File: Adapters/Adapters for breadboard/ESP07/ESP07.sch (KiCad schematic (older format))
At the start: 2 parts, among them J1 Conn_02x08_Counter_Clockwise

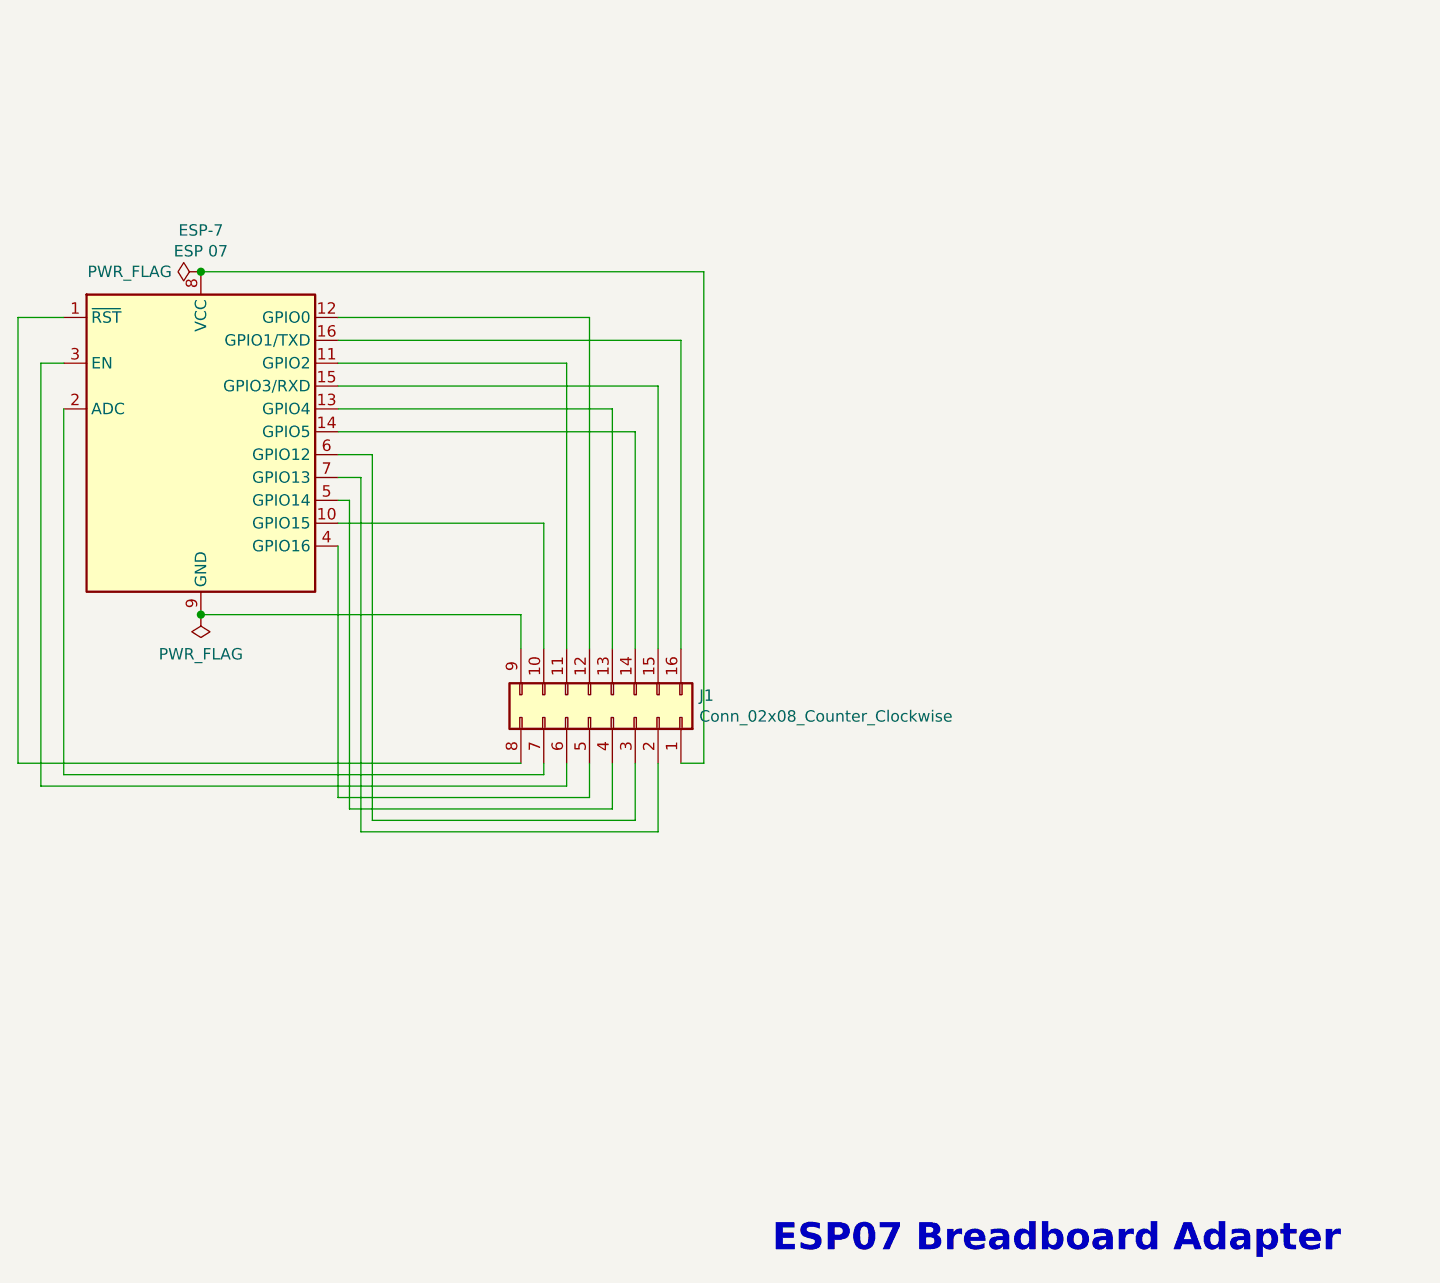
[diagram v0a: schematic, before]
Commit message: Fixed error in ESP breadboard adapter footprint, updated the schema to wire the for the new layout. Updated the ESP flashing adapter.
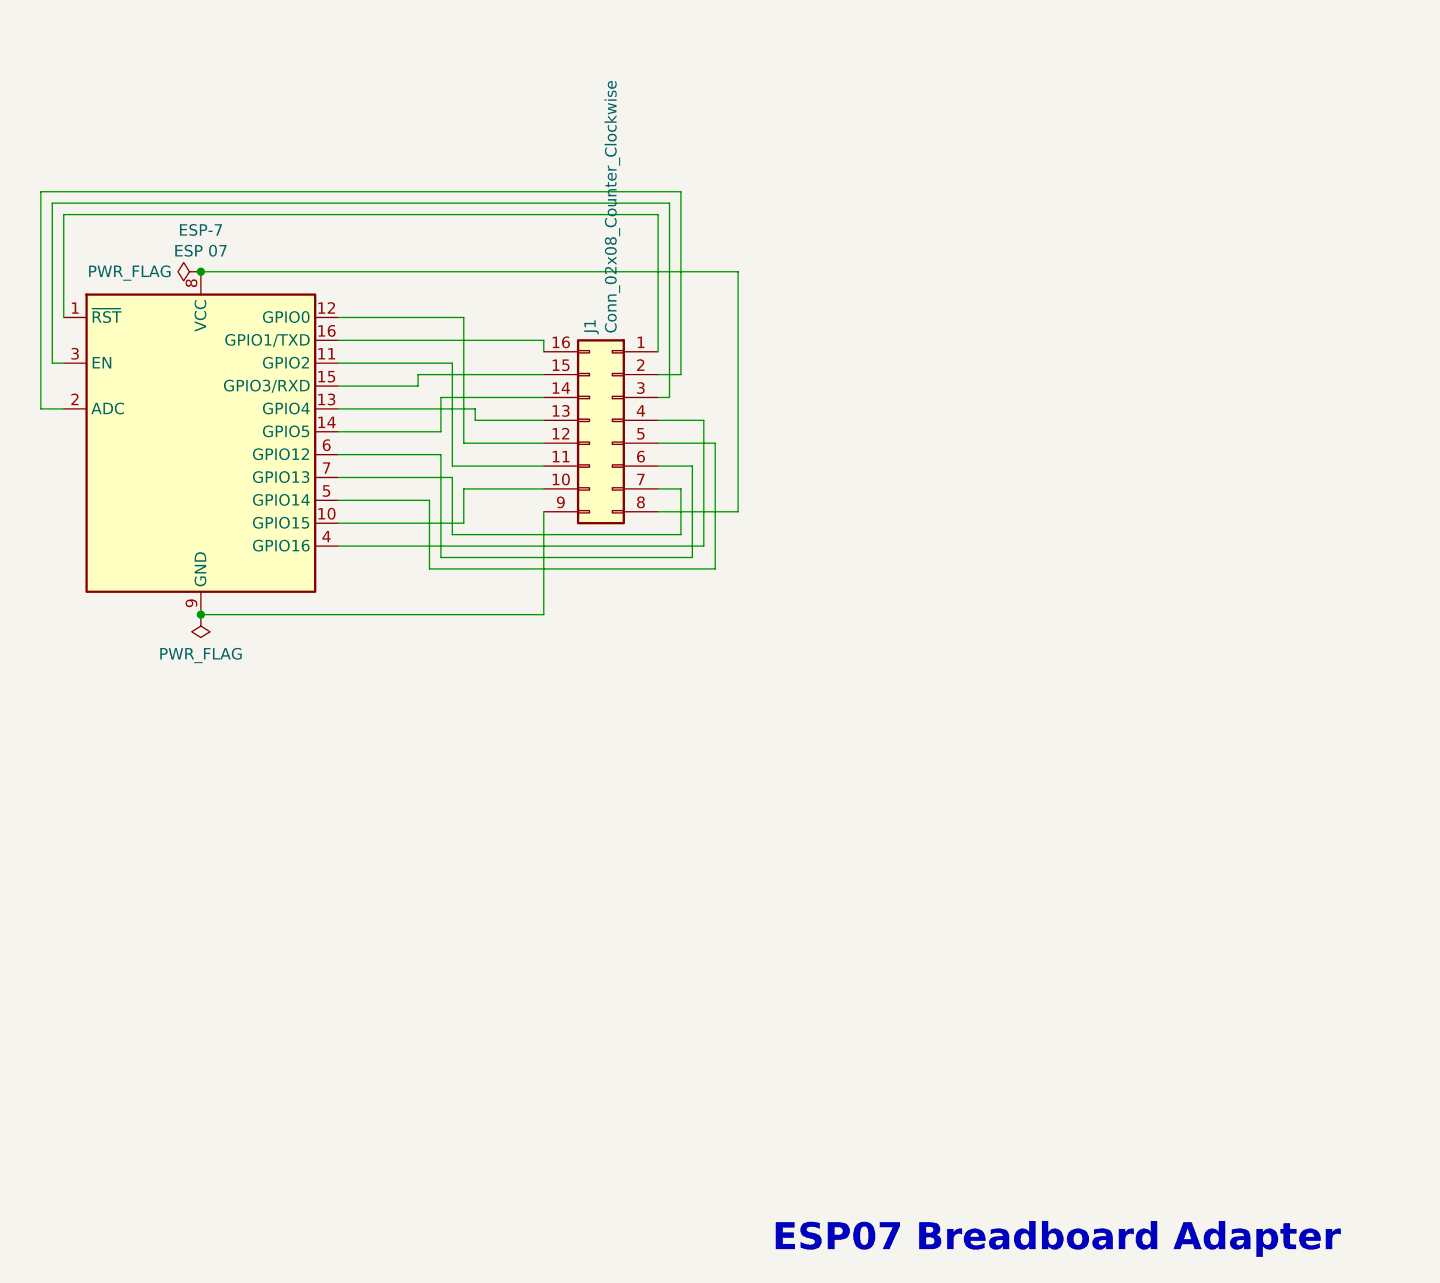
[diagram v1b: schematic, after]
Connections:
- net at ESP-7.1 (~RST): now also J1.1 (Pin_1); no longer J1.8 (Pin_8)
- net at ESP-7.2 (ADC): now also J1.2 (Pin_2); no longer J1.7 (Pin_7)
- net at ESP-7.3 (EN): now also J1.3 (Pin_3); no longer J1.6 (Pin_6)
- net at ESP-7.4 (GPIO16): now also J1.4 (Pin_4); no longer J1.5 (Pin_5)
- net at ESP-7.5 (GPIO14): now also J1.5 (Pin_5); no longer J1.4 (Pin_4)
- net at ESP-7.6 (GPIO12): now also J1.6 (Pin_6); no longer J1.3 (Pin_3)
- net at ESP-7.7 (GPIO13): now also J1.7 (Pin_7); no longer J1.2 (Pin_2)
- net at ESP-7.8 (VCC): now also J1.8 (Pin_8); no longer J1.1 (Pin_1)
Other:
- moved on the sheet: J1
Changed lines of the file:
@@
 L Connector_Generic:Conn_02x08_Counter_Clockwise J1
 U 1 1 5E50BF8B
-P 6300 4500
-F 0 "J1" V 6396 4880 50  0000 L CNN
-F 1 "Conn_02x08_Counter_Clockwise" V 6305 4880 50  0000 L CNN
-F 2 "ArduinoUnoMultiProgrammerAdapters:ESP07BreaboardSocket" H 6300 4500 50  0001 C CNN
-F 3 "~" H 6300 4500 50  0001 C CNN
-	1    6300 4500
-	0    1    -1   0
+P 6300 3200
+F 0 "J1" V 6396 3580 50  0000 L CNN
+F 1 "Conn_02x08_Counter_Clockwise" V 6305 3580 50  0000 L CNN
+F 2 "ArduinoUnoMultiProgrammerAdapters:ESP07BreaboardSocket" H 6300 3200 50  0001 C CNN
+F 3 "~" H 6300 3200 50  0001 C CNN
+	1    6300 3200
+	-1   0    0    -1
 $EndComp
 Wire Wire Line
-	4500 4050 5900 4050
+	3900 2750 3900 2300
 Wire Wire Line
-	5900 4050 5900 4200
+	3900 2300 6500 2300
+Wire Wire Line
+	6500 2300 6500 2900
+Wire Wire Line
+	3900 2950 3850 2950
+Wire Wire Line
+	3850 2950 3850 2250
+Wire Wire Line
+	3850 2250 6550 2250
+Wire Wire Line
+	6550 2250 6550 3100
+Wire Wire Line
+	6550 3100 6500 3100
+Wire Wire Line
+	3900 3150 3800 3150
+Wire Wire Line
+	3800 3150 3800 2200
+Wire Wire Line
+	3800 2200 6600 2200
+Wire Wire Line
+	6600 2200 6600 3000
+Wire Wire Line
+	6600 3000 6500 3000
+Wire Wire Line
+	5100 3750 6700 3750
+Wire Wire Line
+	6700 3750 6700 3200
+Wire Wire Line
+	6700 3200 6500 3200
+Wire Wire Line
+	5100 3550 5500 3550
+Wire Wire Line
+	5500 3550 5500 3850
+Wire Wire Line
+	5500 3850 6750 3850
+Wire Wire Line
+	6750 3850 6750 3300
+Wire Wire Line
+	6750 3300 6500 3300
+Wire Wire Line
+	5100 3350 5550 3350
+Wire Wire Line
+	5550 3350 5550 3800
+Wire Wire Line
+	5550 3800 6650 3800
+Wire Wire Line
+	6650 3800 6650 3400
+Wire Wire Line
+	6650 3400 6500 3400
+Wire Wire Line
+	5100 3450 5600 3450
+Wire Wire Line
+	5600 3450 5600 3700
+Wire Wire Line
+	5600 3700 6600 3700
+Wire Wire Line
+	6600 3700 6600 3500
+Wire Wire Line
+	6600 3500 6500 3500
+Wire Wire Line
+	4500 2550 6850 2550
+Wire Wire Line
+	6850 2550 6850 3600
+Wire Wire Line
+	6850 3600 6500 3600
+Connection ~ 4500 2550
+Wire Wire Line
+	5100 3650 5650 3650
+Wire Wire Line
+	5650 3650 5650 3500
+Wire Wire Line
+	5650 3500 6000 3500
+Wire Wire Line
+	4500 4050 6000 4050
+Wire Wire Line
+	6000 4050 6000 3600
 Connection ~ 4500 4050
 Wire Wire Line
-	5100 3650 6000 3650
+	5100 2950 5600 2950
 Wire Wire Line
-	6000 3650 6000 4200
+	5600 2950 5600 3400
 Wire Wire Line
-	5100 2950 6100 2950
+	5600 3400 6000 3400
 Wire Wire Line
-	6100 2950 6100 4200
+	5100 2750 5650 2750
 Wire Wire Line
-	5100 2750 6200 2750
+	5650 2750 5650 3300
 Wire Wire Line
-	6200 2750 6200 4200
+	5650 3300 6000 3300
 Wire Wire Line
-	5100 3150 6300 3150
+	5100 3150 5700 3150
 Wire Wire Line
-	6300 3150 6300 4200
+	5700 3150 5700 3200
 Wire Wire Line
-	5100 3250 6400 3250
+	5700 3200 6000 3200
 Wire Wire Line
-	6400 3250 6400 4200
+	5100 3250 5550 3250
 Wire Wire Line
-	5100 3050 6500 3050
+	5550 3250 5550 3100
 Wire Wire Line
-	6500 3050 6500 4200
+	5550 3100 6000 3100
 Wire Wire Line
-	5100 2850 6600 2850
+	5100 3050 5450 3050
 Wire Wire Line
-	6600 2850 6600 4200
+	5450 3050 5450 3000
 Wire Wire Line
-	4500 2550 6700 2550
+	5450 3000 6000 3000
 Wire Wire Line
-	6700 2550 6700 4700
+	5100 2850 6000 2850
 Wire Wire Line
-	6700 4700 6600 4700
-Connection ~ 4500 2550
-Wire Wire Line
-	3900 2750 3700 2750
-Wire Wire Line
-	3700 2750 3700 4700
-Wire Wire Line
-	3700 4700 5900 4700
-Wire Wire Line
-	3900 3150 3900 4750
-Wire Wire Line
-	3900 4750 6000 4750
-Wire Wire Line
-	6000 4750 6000 4700
-Wire Wire Line
-	3900 2950 3800 2950
-Wire Wire Line
-	3800 2950 3800 4800
-Wire Wire Line
-	3800 4800 6100 4800
-Wire Wire Line
-	6100 4800 6100 4700
-Wire Wire Line
-	5100 3750 5100 4850
-Wire Wire Line
-	5100 4850 6200 4850
-Wire Wire Line
-	6200 4850 6200 4700
-Wire Wire Line
-	5100 3550 5150 3550
-Wire Wire Line
-	5150 3550 5150 4900
-Wire Wire Line
-	5150 4900 6300 4900
-Wire Wire Line
-	6300 4900 6300 4700
-Wire Wire Line
-	5100 3350 5250 3350
-Wire Wire Line
-	5250 3350 5250 4950
-Wire Wire Line
-	5250 4950 6400 4950
-Wire Wire Line
-	6400 4950 6400 4700
-Wire Wire Line
-	5100 3450 5200 3450
-Wire Wire Line
-	5200 3450 5200 5000
-Wire Wire Line
-	5200 5000 6500 5000
-Wire Wire Line
-	6500 5000 6500 4700
+	6000 2850 6000 2900
 $EndSCHEMATC
